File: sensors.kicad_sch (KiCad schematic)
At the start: 17 parts, among them IC3 ICM-45686, IC4 ICM-45686, IC5 MMC5983MA, U3 BMP581, U5 H3LIS331DLTR

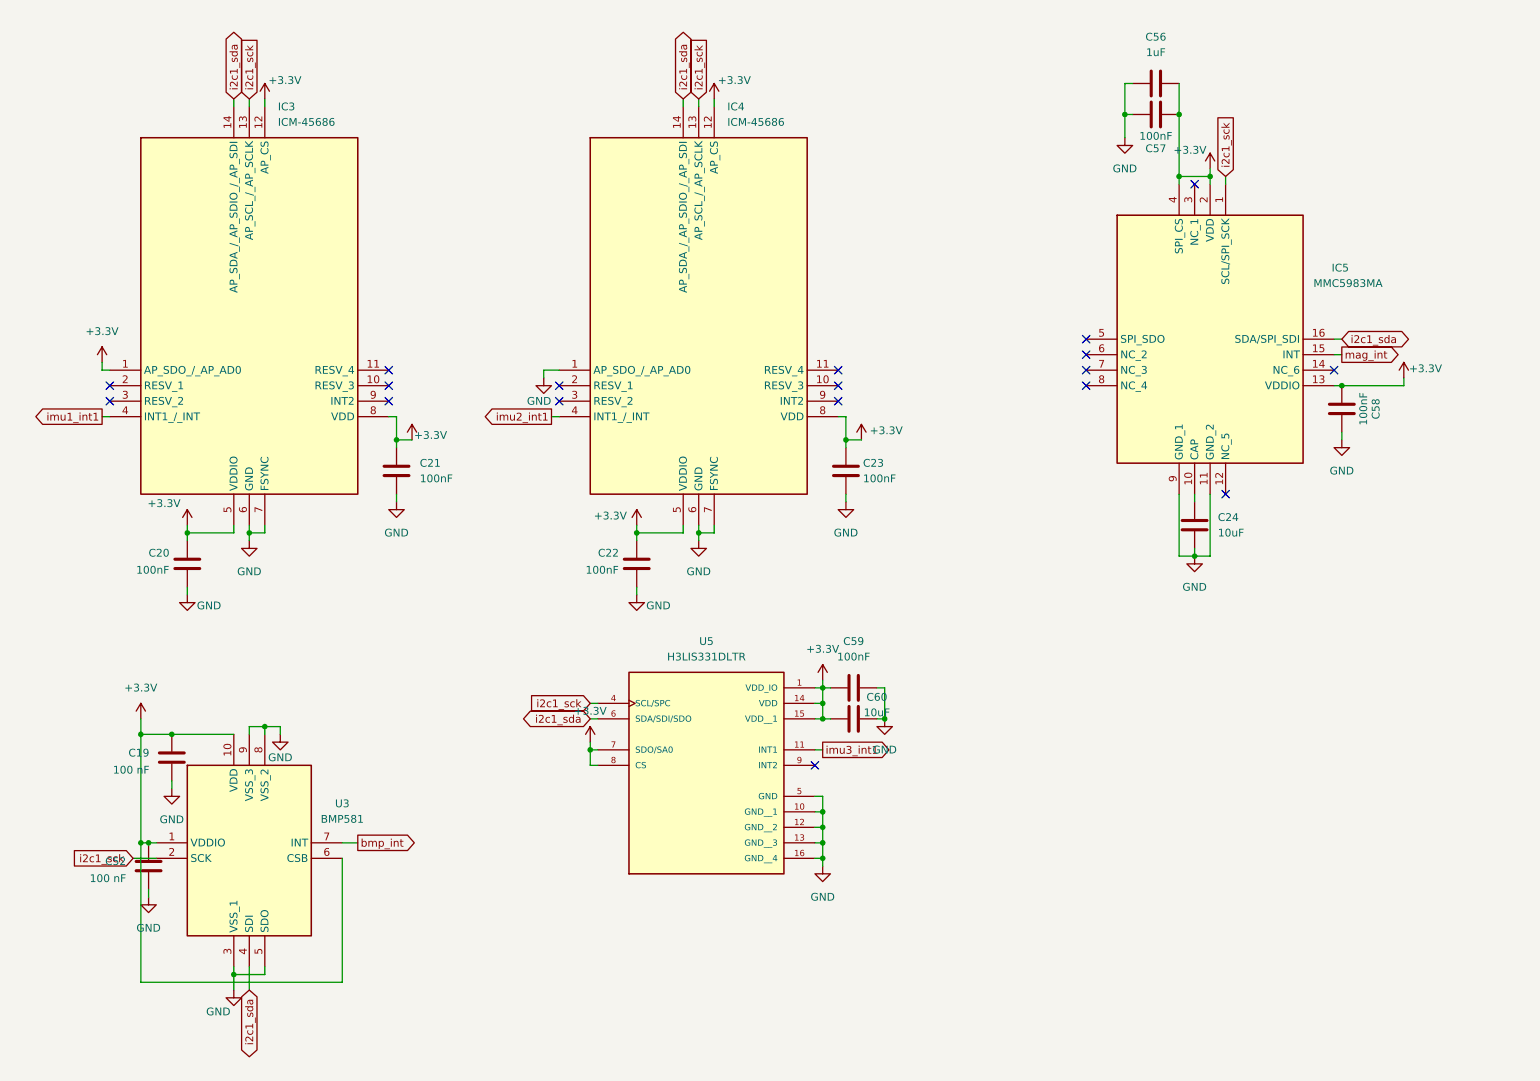
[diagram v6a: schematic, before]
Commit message: started redoing layout for new pinout
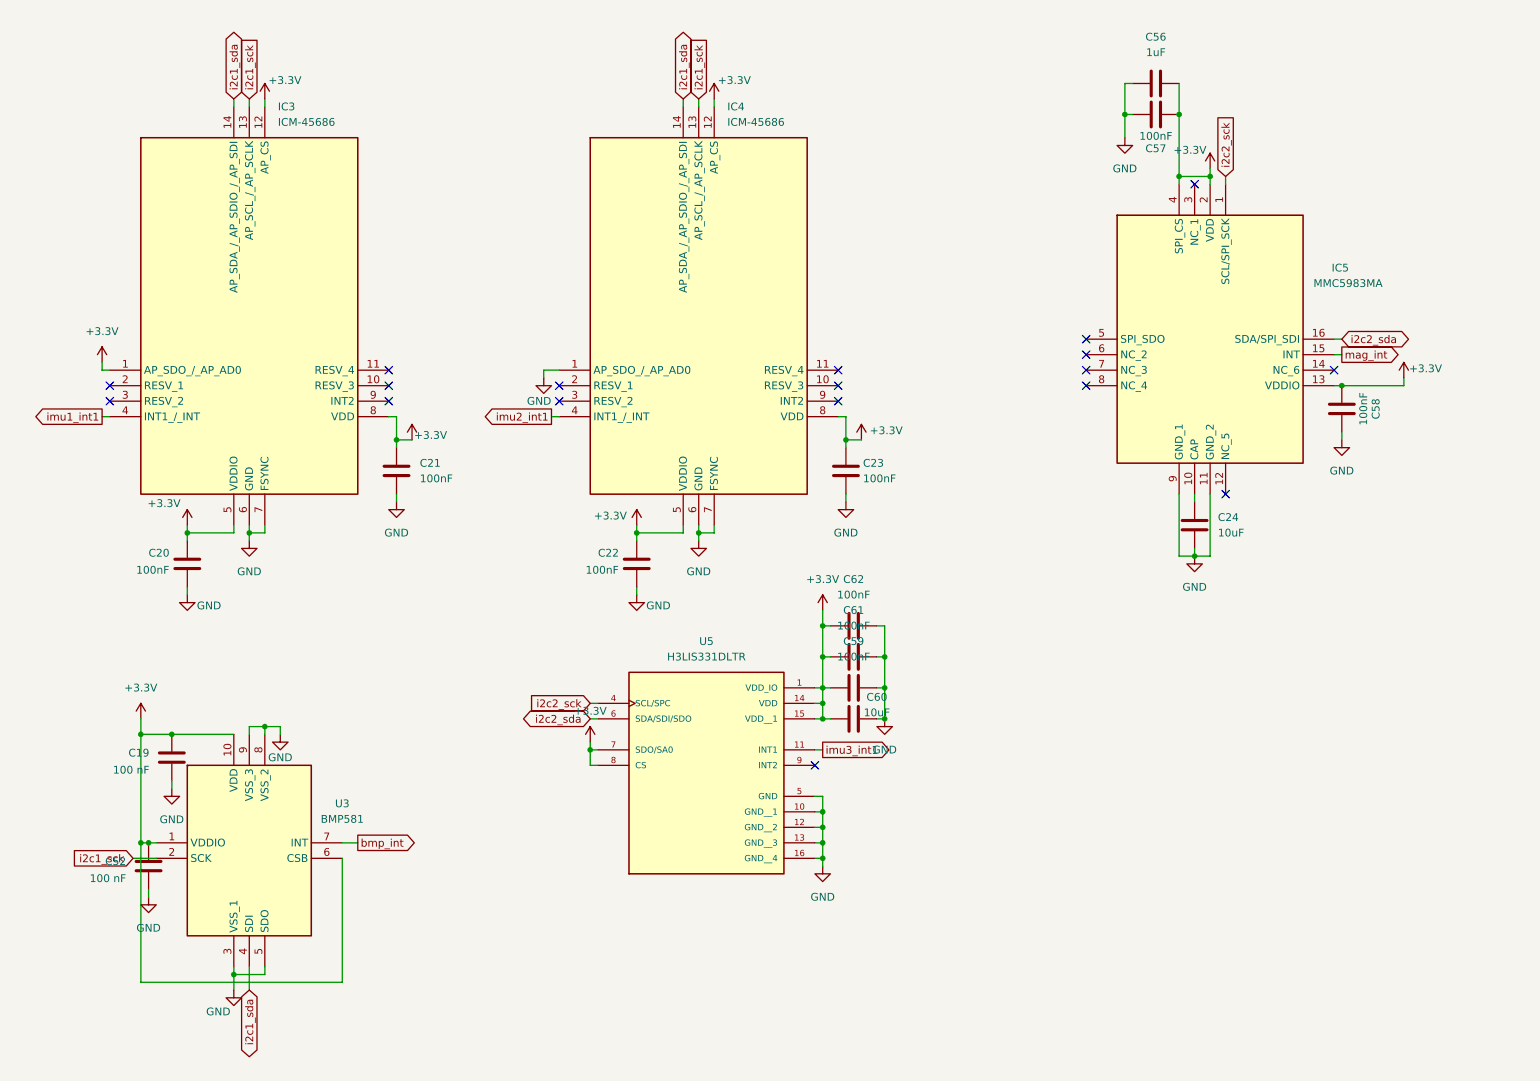
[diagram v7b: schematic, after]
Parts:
- added C61, C62: 100nF, Capacitor_SMD:C_0402_1005Metric, symbol Device:C
- C56, C60: footprint (none) -> Capacitor_SMD:C_0603_1608Metric
- C57, C58, C59: footprint (none) -> Capacitor_SMD:C_0402_1005Metric
- U5: footprint H3LIS331DLTR:QFN300X300X100-16N -> footprints:QFN300X300X100-16N
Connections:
- net +3.3V: now also C61.1, C62.1
- net GND: now also C61.2, C62.2
- net i2c1_sck: no longer IC5.1 (SCL/SPI_SCK), U5.4 (SCL/SPC)
- net i2c1_sda: no longer IC5.16 (SDA/SPI_SDI), U5.6 (SDA/SDI/SDO)
- new net i2c2_sck: IC5.1 (SCL/SPI_SCK), U5.4 (SCL/SPC)
- new net i2c2_sda: IC5.16 (SDA/SPI_SDI), U5.6 (SDA/SDI/SDO)
